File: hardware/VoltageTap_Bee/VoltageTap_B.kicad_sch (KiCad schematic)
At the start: 43 parts, among them J1 Conn_01x09_Socket, J102 Conn_01x18_Pin, J15 Conn_02x04_Odd_Even, J2 Conn_02x05_Odd_Even, Q6 2N7002, SW1 SW_Push, SW2 SW_Push, U2 MCU-MSM0G3507SPM

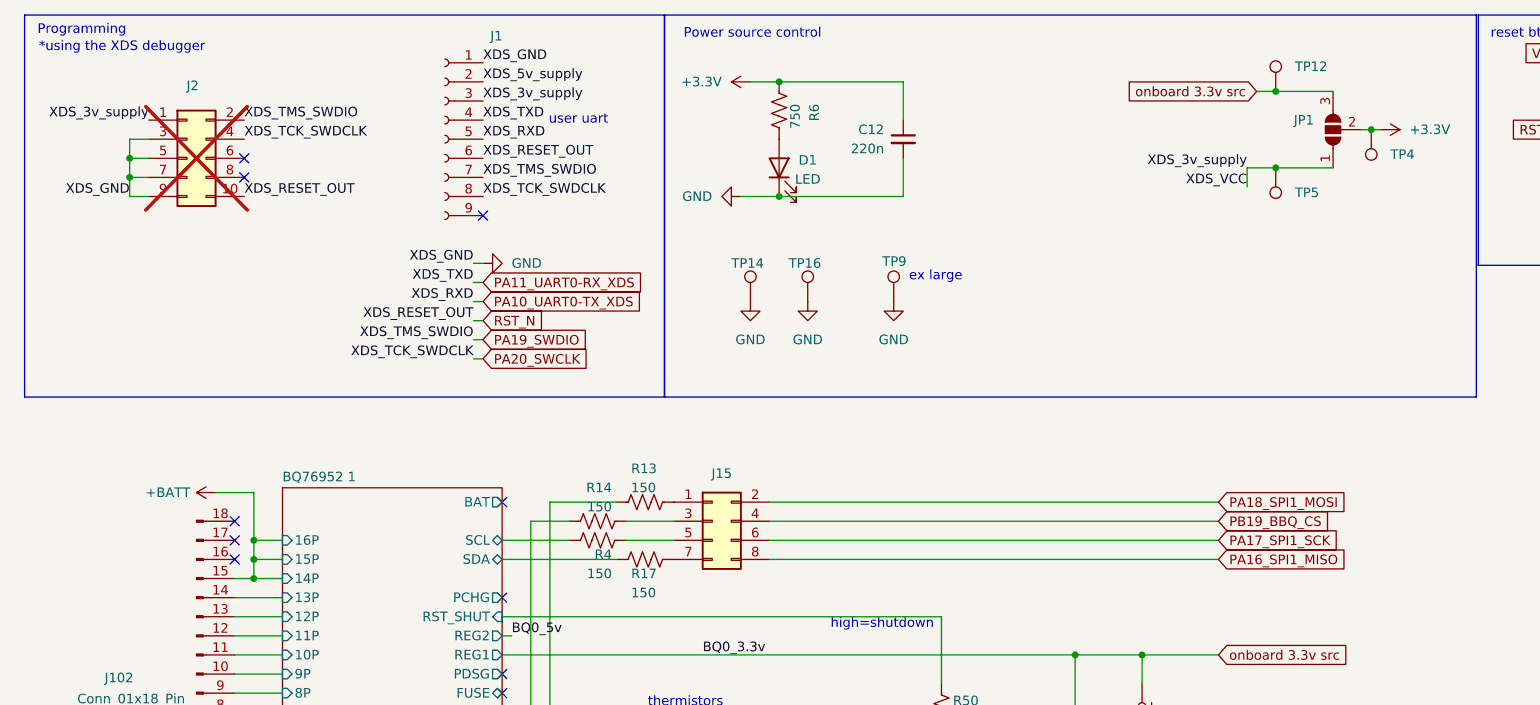
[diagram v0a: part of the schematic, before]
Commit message: VT_BEE changes
need to somehow fit switches, make space
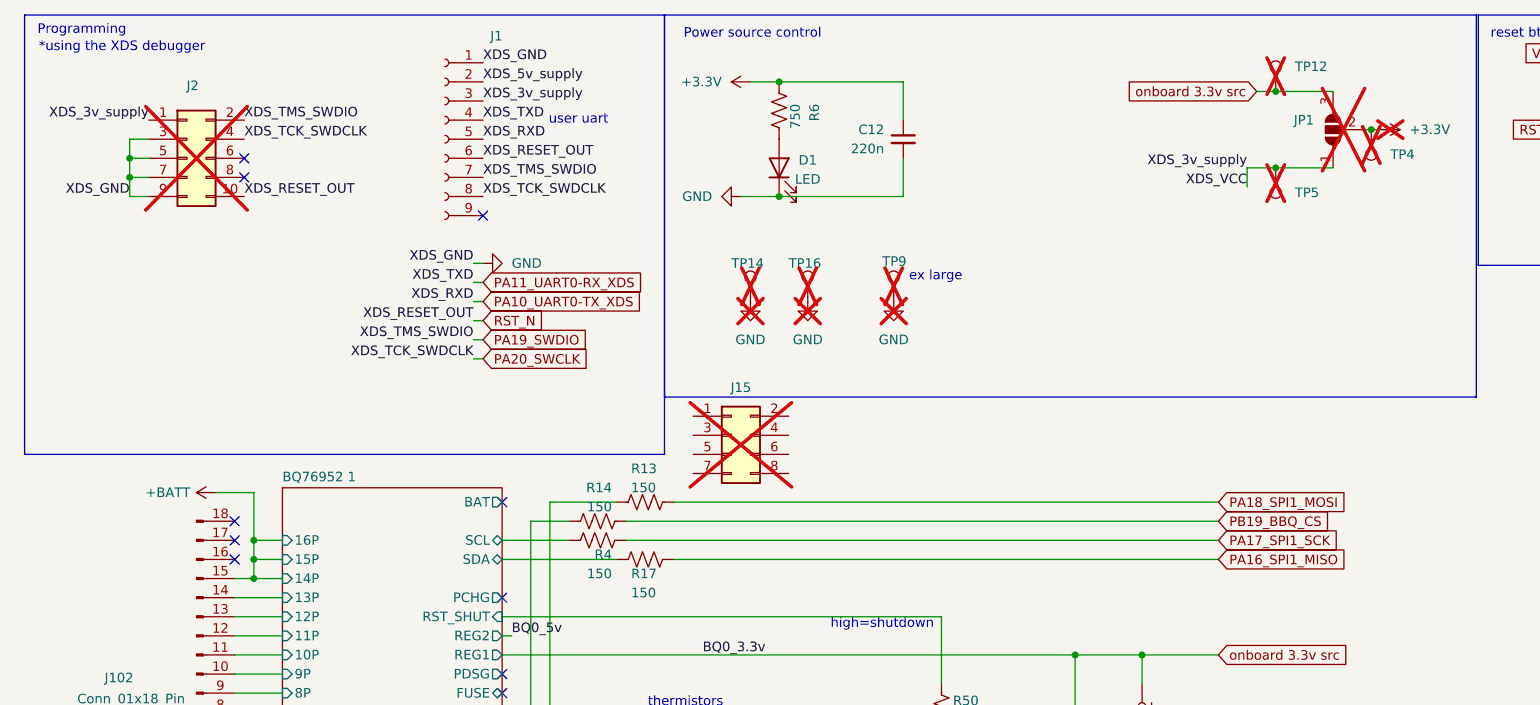
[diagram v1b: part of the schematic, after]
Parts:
- J15, JP1, TP12, TP14, TP16, TP4, TP5, TP9: now not fitted
- SW1, SW2: footprint Button_Switch_SMD:SW_SPST_PTS645 -> Button_Switch_SMD:SW_SPST_PTS645Sx43SMTR92
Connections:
- net PA16_SPI1_MISO: now also R17.1; no longer J15.8 (Pin_8)
- net PA17_SPI1_SCK: now also R4.1; no longer J15.6 (Pin_6)
- net PA18_SPI1_MOSI: now also R13.2; no longer J15.2 (Pin_2)
- net PB19_BBQ_CS: now also R14.2; no longer J15.4 (Pin_4)
- net at J15.5 (Pin_5): no longer R4.1
- net at J15.7 (Pin_7): no longer R17.1
- net at J15.1 (Pin_1): no longer R13.2
- net at J15.3 (Pin_3): no longer R14.2
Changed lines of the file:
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@@
 	(rectangle
 		(start 13.97 15.24)
-		(end 99.06 66.04)
+		(end 99.06 73.66)
 		(stroke
 			(width 0)
@@
 	(wire
 		(pts
-			(xy 93.98 82.55) (xy 100.33 82.55)
+			(xy 93.98 82.55) (xy 172.72 82.55)
 		)
 		(stroke
@@
 	(wire
 		(pts
-			(xy 172.72 87.63) (xy 113.03 87.63)
-		)
-		(stroke
-			(width 0)
-			(type default)
-		)
-	)
-	(wire
-		(pts
 			(xy 44.45 130.81) (xy 48.26 130.81)
 		)
@@
 	(wire
 		(pts
-			(xy 172.72 82.55) (xy 113.03 82.55)
-		)
-		(stroke
-			(width 0)
-			(type default)
-		)
-	)
-	(wire
-		(pts
 			(xy 398.78 198.12) (xy 397.51 198.12)
 		)
@@
 	(wire
 		(pts
-			(xy 172.72 80.01) (xy 113.03 80.01)
-		)
-		(stroke
-			(width 0)
-			(type default)
-		)
-	)
-	(wire
-		(pts
 			(xy 224.79 30.48) (xy 224.79 33.02)
 		)
@@
 	(wire
 		(pts
-			(xy 172.72 85.09) (xy 113.03 85.09)
-		)
-		(stroke
-			(width 0)
-			(type default)
-		)
-	)
-	(wire
-		(pts
 			(xy 162.56 100.33) (xy 172.72 100.33)
 		)
@@
 	(wire
 		(pts
+			(xy 100.33 80.01) (xy 172.72 80.01)
+		)
+		(stroke
+			(width 0)
+			(type default)
+		)
+	)
+	(wire
+		(pts
 			(xy 317.5 35.56) (xy 317.5 39.37)
 		)
@@
 	(wire
 		(pts
+			(xy 100.33 87.63) (xy 172.72 87.63)
+		)
+		(stroke
+			(width 0)
+			(type default)
+		)
+	)
+	(wire
+		(pts
 			(xy 41.91 123.19) (xy 48.26 123.19)
 		)
@@
 	(wire
 		(pts
-			(xy 93.98 85.09) (xy 100.33 85.09)
+			(xy 93.98 85.09) (xy 172.72 85.09)
 		)
 		(stroke
@@
 			)
 		)
-		(property "Footprint" "Button_Switch_SMD:SW_SPST_PTS645"
+		(property "Footprint" "Button_Switch_SMD:SW_SPST_PTS645Sx43SMTR92"
 			(at 167.64 109.22 0)
 			(effects
@@
 		(exclude_from_sim no)
 		(in_bom yes)
-		(on_board yes)
-		(dnp no)
+		(on_board no)
+		(dnp yes)
 		(fields_autoplaced yes)
 		(property "Reference" "#PWR05"
@@
 			)
 		)
-		(property "Footprint" "Button_Switch_SMD:SW_SPST_PTS645"
+		(property "Footprint" "Button_Switch_SMD:SW_SPST_PTS645Sx43SMTR92"
 			(at 236.22 35.56 0)
 			(effects
@@
 		(exclude_from_sim no)
 		(in_bom no)
-		(on_board yes)
-		(dnp no)
+		(on_board no)
+		(dnp yes)
 		(property "Reference" "TP14"
 			(at 107.95 48.26 0)
@@
 		(exclude_from_sim no)
 		(in_bom no)
-		(on_board yes)
-		(dnp no)
+		(on_board no)
+		(dnp yes)
 		(property "Reference" "TP9"
 			(at 128.016 48.006 0)
@@
 		(exclude_from_sim no)
 		(in_bom no)
-		(on_board yes)
-		(dnp no)
+		(on_board no)
+		(dnp yes)
 		(fields_autoplaced yes)
 		(property "Reference" "TP4"
@@
 		(exclude_from_sim no)
 		(in_bom yes)
-		(on_board yes)
+		(on_board no)
 		(dnp yes)
 		(property "Reference" "J2"
@@
 		(exclude_from_sim no)
 		(in_bom no)
-		(on_board yes)
-		(dnp no)
+		(on_board no)
+		(dnp yes)
 		(fields_autoplaced yes)
 		(property "Reference" "TP12"
@@
 		(exclude_from_sim no)
 		(in_bom no)
-		(on_board yes)
-		(dnp no)
+		(on_board no)
+		(dnp yes)
 		(property "Reference" "TP16"
 			(at 115.57 48.26 0)
@@
 		(exclude_from_sim no)
 		(in_bom yes)
-		(on_board yes)
-		(dnp no)
+		(on_board no)
+		(dnp yes)
 		(fields_autoplaced yes)
 		(property "Reference" "#PWR033"
@@
 		(exclude_from_sim no)
 		(in_bom no)
-		(on_board yes)
-		(dnp no)
+		(on_board no)
+		(dnp yes)
 		(fields_autoplaced yes)
 		(property "Reference" "JP1"
@@
 		(exclude_from_sim no)
 		(in_bom yes)
-		(on_board yes)
-		(dnp no)
+		(on_board no)
+		(dnp yes)
 		(fields_autoplaced yes)
 		(property "Reference" "#PWR025"
@@
 		(exclude_from_sim no)
 		(in_bom no)
-		(on_board yes)
-		(dnp no)
+		(on_board no)
+		(dnp yes)
 		(fields_autoplaced yes)
 		(property "Reference" "TP5"
@@
 	(symbol
 		(lib_id "Connector_Generic:Conn_02x04_Odd_Even")
-		(at 105.41 82.55 0)
+		(at 107.95 71.12 0)
 		(unit 1)
 		(exclude_from_sim no)
 		(in_bom yes)
-		(on_board yes)
-		(dnp no)
+		(on_board no)
+		(dnp yes)
 		(fields_autoplaced yes)
 		(property "Reference" "J15"
-			(at 106.68 76.2 0)
+			(at 109.22 64.77 0)
 			(effects
 				(font
@@
 		)
 		(property "Value" "Conn_02x04_Odd_Even"
-			(at 106.68 76.2 0)
+			(at 109.22 64.77 0)
 			(effects
 				(font
@@
 		)
 		(property "Footprint" "Connector_PinHeader_2.54mm:PinHeader_2x04_P2.54mm_Vertical"
-			(at 105.41 82.55 0)
+			(at 107.95 71.12 0)
 			(effects
 				(font
@@
 		)
 		(property "Datasheet" "~"
-			(at 105.41 82.55 0)
+			(at 107.95 71.12 0)
 			(effects
 				(font
@@
 		)
 		(property "Description" "Generic connector, double row, 02x04, odd/even pin numbering scheme (row 1 odd numbers, row 2 even numbers), script generated (kicad-library-utils/schlib/autogen/connector/)"
-			(at 105.41 82.55 0)
+			(at 107.95 71.12 0)
 			(effects
 				(font
@@
 		(exclude_from_sim no)
 		(in_bom yes)
-		(on_board yes)
-		(dnp no)
+		(on_board no)
+		(dnp yes)
 		(fields_autoplaced yes)
 		(property "Reference" "#PWR03"

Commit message: This is a cry for help
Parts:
- removed SW2: SW_Push, Button_Switch_SMD:SW_SPST_PTS645Sx43SMTR92, symbol Switch:SW_Push
- JP1: now fitted; now in the parts list
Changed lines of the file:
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@@
 	)
 	(junction
-		(at 162.56 100.33)
-		(diameter 0)
-		(color 0 0 0 0)
-	)
-	(junction
 		(at 135.89 114.3)
 		(diameter 0)
@@
 	(wire
 		(pts
-			(xy 153.67 100.33) (xy 162.56 100.33)
+			(xy 153.67 100.33) (xy 172.72 100.33)
 		)
 		(stroke
@@
 	(wire
 		(pts
-			(xy 162.56 114.3) (xy 162.56 123.19)
-		)
-		(stroke
-			(width 0)
-			(type default)
-		)
-	)
-	(wire
-		(pts
 			(xy 77.47 87.63) (xy 92.71 87.63)
 		)
@@
 	(wire
 		(pts
-			(xy 162.56 100.33) (xy 172.72 100.33)
-		)
-		(stroke
-			(width 0)
-			(type default)
-		)
-	)
-	(wire
-		(pts
 			(xy 96.52 114.3) (xy 88.9 114.3)
 		)
@@
 	(wire
 		(pts
-			(xy 162.56 100.33) (xy 162.56 104.14)
-		)
-		(stroke
-			(width 0)
-			(type default)
-		)
-	)
-	(wire
-		(pts
 			(xy 162.56 133.35) (xy 162.56 143.51)
 		)
@@
 	)
 	(symbol
-		(lib_id "Switch:SW_Push")
-		(at 162.56 109.22 270)
-		(unit 1)
-		(exclude_from_sim no)
-		(in_bom yes)
-		(on_board yes)
-		(dnp no)
-		(fields_autoplaced yes)
-		(property "Reference" "SW2"
-			(at 166.37 107.9499 90)
-			(effects
-				(font
-					(size 1.27 1.27)
-				)
-				(justify left)
-			)
-		)
-		(property "Value" "SW_Push"
-			(at 166.37 110.4899 90)
-			(effects
-				(font
-					(size 1.27 1.27)
-				)
-				(justify left)
-			)
-		)
-		(property "Footprint" "Button_Switch_SMD:SW_SPST_PTS645Sx43SMTR92"
-			(at 167.64 109.22 0)
-			(effects
-				(font
-					(size 1.27 1.27)
-				)
-				(hide yes)
-			)
-		)
-		(property "Datasheet" "https://www.mouser.com/ProductDetail/Soldered/101111?qs=%252BXxaIXUDbq05T1Vr5nLouw%3D%3D"
-			(at 167.64 109.22 0)
-			(effects
-				(font
-					(size 1.27 1.27)
-				)
-				(hide yes)
-			)
-		)
-		(property "Description" "Push button switch, generic, two pins"
-			(at 162.56 109.22 0)
-			(effects
-				(font
-					(size 1.27 1.27)
-				)
-				(hide yes)
-			)
-		)
-		(property "Sim.Device" ""
-			(at 162.56 109.22 90)
-			(effects
-				(font
-					(size 1.27 1.27)
-				)
-				(hide yes)
-			)
-		)
-		(property "Sim.Type" ""
-			(at 162.56 109.22 90)
-			(effects
-				(font
-					(size 1.27 1.27)
-				)
-				(hide yes)
-			)
-		)
-		(property "mouser" "https://www.mouser.com/ProductDetail/CK/KSC251J-SP-DELTA-LFS?qs=sGAEpiMZZMtFyPk3yBMYYFTocizRX9VpYSHB0QfEbpY%3D"
-			(at 162.56 109.22 90)
-			(effects
-				(font
-					(size 1.27 1.27)
-				)
-				(hide yes)
-			)
-		)
-		(property "unit x10" "0.532"
-			(at 162.56 109.22 90)
-			(effects
-				(font
-					(size 1.27 1.27)
-				)
-				(hide yes)
-			)
-		)
-		(pin "2"
-		)
-		(pin "1"
-		)
-		(instances
-			(project "VoltageTap_B"
-				(path "/24c6cb45-cbeb-4148-a23c-ec2e76234670"
-					(reference "SW2")
-					(unit 1)
-				)
-			)
-		)
-	)
-	(symbol
 		(lib_id "power:GND")
 		(at 224.79 40.64 0)
@@
 		(unit 1)
 		(exclude_from_sim no)
-		(in_bom no)
-		(on_board no)
-		(dnp yes)
+		(in_bom yes)
+		(on_board yes)
+		(dnp no)
 		(fields_autoplaced yes)
 		(property "Reference" "JP1"
@@
 		(exclude_from_sim no)
 		(in_bom yes)
-		(on_board no)
-		(dnp yes)
+		(on_board yes)
+		(dnp no)
 		(fields_autoplaced yes)
 		(property "Reference" "#PWR025"

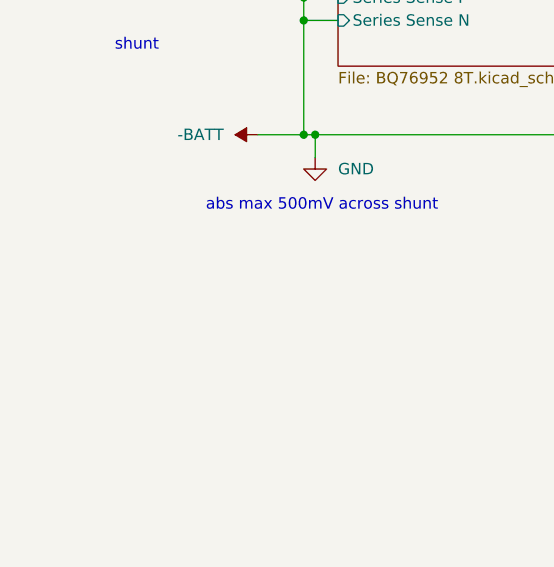
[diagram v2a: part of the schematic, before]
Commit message: added mounting hole and going to change some params
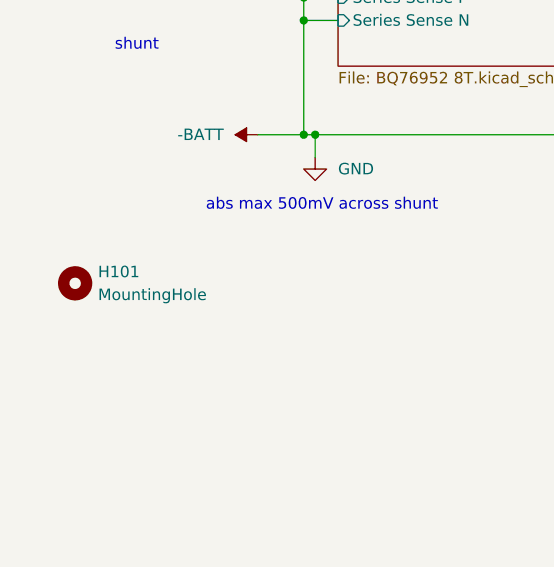
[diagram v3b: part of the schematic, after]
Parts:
- added H101: MountingHole, MountingHole:MountingHole_3.2mm_M3, symbol Mechanical:MountingHole
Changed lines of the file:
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@@
+	)
+	(symbol
+		(lib_id "Mechanical:MountingHole")
+		(at 19.05 160.02 0)
+		(unit 1)
+		(exclude_from_sim no)
+		(in_bom no)
+		(on_board yes)
+		(dnp no)
+		(fields_autoplaced yes)
+		(property "Reference" "H101"
+			(at 21.59 158.7499 0)
+			(effects
+				(font
+					(size 1.27 1.27)
+				)
+				(justify left)
+			)
+		)
+		(property "Value" "MountingHole"
+			(at 21.59 161.2899 0)
+			(effects
+				(font
+					(size 1.27 1.27)
+				)
+				(justify left)
+			)
+		)
+		(property "Footprint" "MountingHole:MountingHole_3.2mm_M3"
+			(at 19.05 160.02 0)
+			(effects
+				(font
+					(size 1.27 1.27)
+				)
+				(hide yes)
+			)
+		)
+		(property "Datasheet" "~"
+			(at 19.05 160.02 0)
+			(effects
+				(font
+					(size 1.27 1.27)
+				)
+				(hide yes)
+			)
+		)
+		(property "Description" "Mounting Hole without connection"
+			(at 19.05 160.02 0)
+			(effects
+				(font
+					(size 1.27 1.27)
+				)
+				(hide yes)
+			)
+		)
+		(property "Sim.Pins" ""
+			(at 19.05 160.02 0)
+			(effects
+				(font
+					(size 1.27 1.27)
+				)
+				(hide yes)
+			)
+		)
+		(property "note" ""
+			(at 19.05 160.02 0)
+			(effects
+				(font
+					(size 1.27 1.27)
+				)
+				(hide yes)
+			)
+		)
+		(instances
+			(project "VoltageTap_B"
+				(path "/24c6cb45-cbeb-4148-a23c-ec2e76234670"
+					(reference "H101")
+					(unit 1)
+				)
+			)
+		)
 	)
 	(symbol

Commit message: uhhh part 2
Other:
- sheet GLV interface renamed (lib_symbols 	(symbol "Regulator_Linear:AP7384-50SA" 		(pin_names 			(offset 0.254) 		) 		(exclude_from_sim no) 		(in_bom yes) 		(on_board yes) 		(property "Reference" "U" 			(at -3.81 3.175 0) 			(effects 				(font (size 1.27 1.27)) 			) 		) 		(property "Value" "AP7384-50SA" 			(at 0 3.175 0) 			(effects 				(font (size 1.27 1.27)) 				(justify left) 			) 		) 		(property "Footprint" "Package_TO_SOT_SMD:SOT-23" 			(at 0 5.715 0) 			(effects 				(font (size 1.27 1.27) (italic yes)) 				(hide yes) 			) 		) 		(property "Datasheet" "https://www.diodes.com/assets/Datasheets/AP7384.pdf" 			(at 0 -1.27 0) 			(effects 				(font (size 1.27 1.27)) 				(hide yes) 			) 		) 		(property "Description" "50mA Low Dropout Voltage Regulator, Fixed Output 5V, Wide Input Voltage Range 40V, SOT-23" 			(at 0 0 0) 			(effects 				(font (size 1.27 1.27)) 				(hide yes) 			) 		) 		(property "ki_keywords" "50mA LDO Regulator Fixed Positive" 			(at 0 0 0) 			(effects 				(font (size 1.27 1.27)) 				(hide yes) 			) 		) 		(property "ki_fp_filters" "SOT?23*" 			(at 0 0 0) 			(effects 				(font (size 1.27 1.27)) 				(hide yes) 			) 		) 		(symbol "AP7384-50SA_0_1" 			(rectangle 				(start -5.08 1.905) 				(end 5.08 -5.08) 				(stroke (width 0.254) (type default)) 				(fill (type background)) 			) 		) 		(symbol "AP7384-50SA_1_1" 			(pin power_in line 				(at -7.62 0 0) 				(length 2.54) 				(name "VI" 					(effects 						(font (size 1.27 1.27)) 					) 				) 				(number "1" 					(effects 						(font (size 1.27 1.27)) 					) 				) 			) 			(pin power_in line 				(at 0 -7.62 90) 				(length 2.54) 				(name "GND" 					(effects 						(font (size 1.27 1.27)) 					) 				) 				(number "3" 					(effects 						(font (size 1.27 1.27)) 					) 				) 			) 			(pin power_out line 				(at 7.62 0 180) 				(length 2.54) 				(name "VO" 					(effects 						(font (size 1.27 1.27)) 					) 				) 				(number "2" 					(effects 						(font (size 1.27 1.27)) 					) 				) 			) 		) 		(embedded_fonts no) 	) ) (symbol 	(lib_id "Regulator_Linear:AP7384-50SA") 	(at 270.51 26.67 0) 	(unit 1) 	(exclude_from_sim no) 	(in_bom yes) 	(on_board yes) 	(dnp no) 	(fields_autoplaced yes) 	(uuid "63645a03-0dcf-4de9-9155-a6ccb0705d23") 	(property "Reference" "U26" 		(at 270.51 20.32 0) 		(effects 			(font (size 1.27 1.27)) 		) 	) 	(property "Value" "AP7384-50SA" 		(at 270.51 22.86 0) 		(effects 			(font (size 1.27 1.27)) 		) 	) 	(property "Footprint" "Package_TO_SOT_SMD:SOT-23" 		(at 270.51 20.955 0) 		(effects 			(font (size 1.27 1.27) (italic yes)) 			(hide yes) 		) 	) 	(property "Datasheet" "https://www.diodes.com/assets/Datasheets/AP7384.pdf" 		(at 270.51 27.94 0) 		(effects 			(font (size 1.27 1.27)) 			(hide yes) 		) 	) 	(property "Description" "50mA Low Dropout Voltage Regulator, Fixed Output 5V, Wide Input Voltage Range 40V, SOT-23" 		(at 270.51 26.67 0) 		(effects 			(font (size 1.27 1.27)) 			(hide yes) 		) 	) 	(property "mouser" "https://www.mouser.com/ProductDetail/Diodes-Incorporated/AP7375-50SA-7?qs=t7xnP681wgX8yYKy1Pe5iA%3D%3D" 		(at 270.51 26.67 0) 		(effects 			(font (size 1.27 1.27)) 			(hide yes) 		) 	) 	(property "unit x1" "0.25" 		(at 270.51 26.67 0) 		(effects 			(font (size 1.27 1.27)) 			(hide yes) 		) 	) 	(property "unit x10" "0.174" 		(at 270.51 26.67 0) 		(effects 			(font (size 1.27 1.27)) 			(hide yes) 		) 	) 	(property "unit x25" "0.154" 		(at 270.51 26.67 0) 		(effects 			(font (size 1.27 1.27)) 			(hide yes) 		) 	) 	(pin "3" 		(uuid "9ddd95e1-ca1e-416e-9dfe-24d7a0b4d0e6") 	) 	(pin "2" 		(uuid "ab10e457-2625-421f-8a82-9adf340550bb") 	) 	(pin "1" 		(uuid "b619a3b1-fac7-4971-8cb9-ac4027e9c86d") 	) 	(instances 		(project "VoltageTap_B" 			(path "" 				(reference "U26") 				(unit 1) 			) 			(path "/24c6cb45-cbeb-4148-a23c-ec2e76234670/443e7a8e-9df5-428f-9d56-3f2b4e9a9ffe/50286653-b14c-419a-bf32-2b9dde1a77b3" 				(reference "U46") 				(unit 1) 			) 		) 	) )
- added sheet something (../common designs.kicad_sch)
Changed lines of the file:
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@@
+	)
+	(sheet
+		(at 426.72 194.31)
+		(size 27.94 22.86)
+		(exclude_from_sim yes)
+		(in_bom no)
+		(on_board no)
+		(dnp yes)
+		(fields_autoplaced yes)
+		(stroke
+			(width 0.1524)
+			(type solid)
+		)
+		(fill
+			(color 0 0 0 0.0000)
+		)
+		(property "Sheetname" "something"
+			(at 426.72 193.5984 0)
+			(effects
+				(font
+					(size 1.27 1.27)
+				)
+				(justify left bottom)
+			)
+		)
+		(property "Sheetfile" "../common designs.kicad_sch"
+			(at 426.72 217.7546 0)
+			(effects
+				(font
+					(size 1.27 1.27)
+				)
+				(justify left top)
+			)
+		)
+		(property "Field2" ""
+			(at 426.72 194.31 0)
+			(effects
+				(font
+					(size 1.27 1.27)
+				)
+			)
+		)
+		(instances
+			(project "VoltageTap_B"
+				(path "/24c6cb45-cbeb-4148-a23c-ec2e76234670"
+					(page "5")
+				)
+			)
+		)
 	)
 	(sheet
@@
 			(color 0 0 0 0.0000)
 		)
-		(property "Sheetname" "GLV interface"
-			(at 336.55 226.6184 0)
-			(effects
-				(font
-					(size 1.27 1.27)
-				)
-				(justify left bottom)
-			)
-		)
 		(property "Sheetfile" "GLV CAN TRX.kicad_sch"
